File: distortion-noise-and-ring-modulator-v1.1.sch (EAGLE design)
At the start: 74 parts, among them IC1 TL074JT, IC4 LM13700SL, IC5 TL074JT, Q1 MMBT3906, T1 NOISE-2N3904, U1 MC1496DR2G, X1 MA07-1JN, X4 MA07-1JN

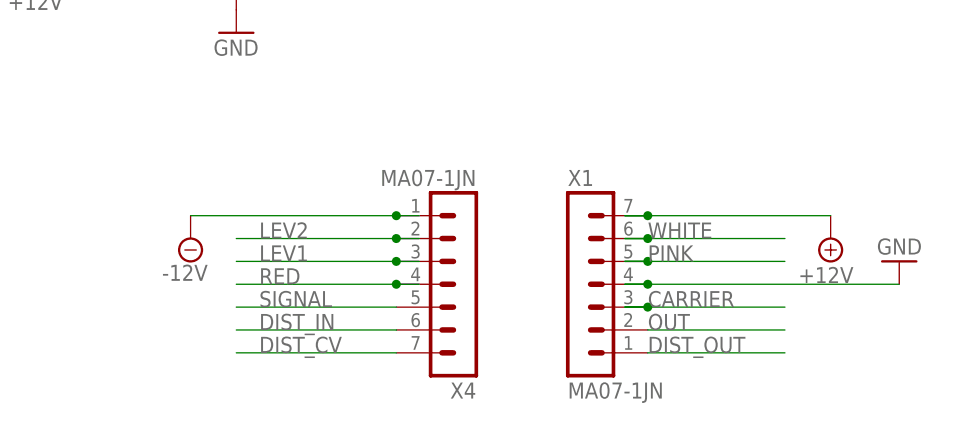
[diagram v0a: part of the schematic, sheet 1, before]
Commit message: Removed all external trimmers
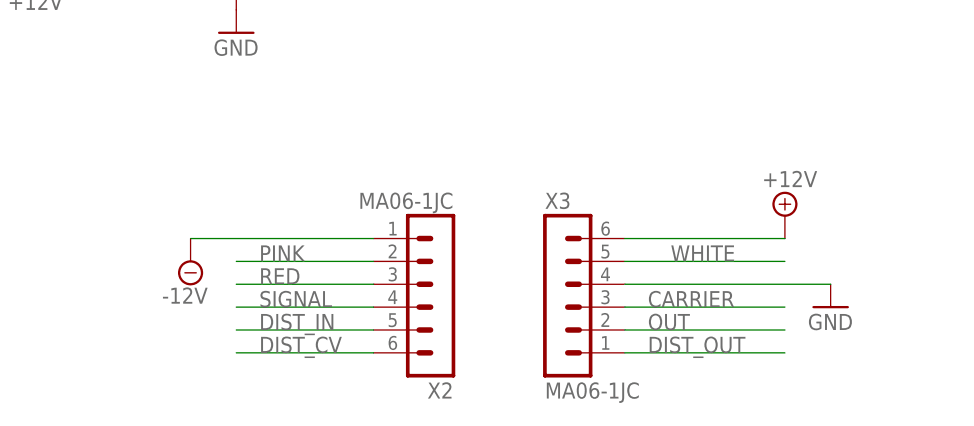
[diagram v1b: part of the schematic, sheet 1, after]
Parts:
- removed X1, X4: MA07-1JN, joakim:MA07-1JN
- added X2, X3: MA06-1JC, joakim:MA06-1JC
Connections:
- net +12V: now also X3.6; no longer X1.7
- net -12V: now also X2.1; no longer X4.1
- net CARRIER: now also X3.3; no longer X1.3
- net DIST_CV: now also X2.6; no longer X4.7
- net DIST_IN: now also X2.5; no longer X4.6
- net DIST_OUT: now also X3.1; no longer X1.1
- net GND: now also X3.4; no longer X1.4
- net LEV1: no longer X4.3
- net LEV2: no longer X4.2
- net OUT: now also X3.2; no longer X1.2
- net PINK: now also X2.2; no longer X1.5
- net RED: now also X2.3; no longer X4.4
- net SIGNAL: now also X2.4; no longer X4.5
- net WHITE: now also X3.5; no longer X1.6
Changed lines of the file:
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@@
 <part name="SUPPLY15" library="supply2" library_urn="urn:adsk.eagle:library:372" deviceset="-12V" device=""/>
 <part name="SUPPLY16" library="supply2" library_urn="urn:adsk.eagle:library:372" deviceset="+12V" device=""/>
-<part name="X1" library="joakim" deviceset="MA07-1J" device="N"/>
-<part name="X4" library="joakim" deviceset="MA07-1J" device="N"/>
+<part name="X2" library="joakim" deviceset="MA06-1J" device="C"/>
+<part name="X3" library="joakim" deviceset="MA06-1J" device="C"/>
 </parts>
 <sheets>
@@
 <attribute name="VALUE" x="-47.244" y="40.259" size="1.778" layer="96" rot="R180"/>
 </instance>
-<instance part="GND8" gate="1" x="180.34" y="27.94" smashed="yes" rot="R180">
-<attribute name="VALUE" x="182.88" y="30.48" size="1.778" layer="96" rot="R180"/>
+<instance part="GND8" gate="1" x="172.72" y="22.86" smashed="yes">
+<attribute name="VALUE" x="170.18" y="20.32" size="1.778" layer="96"/>
 </instance>
 <instance part="SUPPLY1" gate="+12V" x="-30.48" y="48.26" smashed="yes">
@@
 <attribute name="VALUE" x="78.74" y="66.675" size="1.778" layer="96"/>
 </instance>
-<instance part="SUPPLY9" gate="G$1" x="101.6" y="30.48" smashed="yes">
-<attribute name="VALUE" x="98.425" y="25.781" size="1.778" layer="96"/>
+<instance part="SUPPLY9" gate="G$1" x="101.6" y="27.94" smashed="yes">
+<attribute name="VALUE" x="98.425" y="23.241" size="1.778" layer="96"/>
 </instance>
 <instance part="SUPPLY10" gate="G$1" x="38.1" y="27.94" smashed="yes">
 <attribute name="VALUE" x="34.925" y="23.241" size="1.778" layer="96"/>
 </instance>
-<instance part="SUPPLY11" gate="+12V" x="172.72" y="30.48" smashed="yes" rot="R180">
-<attribute name="VALUE" x="175.26" y="27.305" size="1.778" layer="96" rot="R180"/>
+<instance part="SUPPLY11" gate="+12V" x="167.64" y="33.02" smashed="yes">
+<attribute name="VALUE" x="165.1" y="36.195" size="1.778" layer="96"/>
 </instance>
 <instance part="IC5" gate="B" x="139.7" y="71.12" smashed="yes">
@@
 <attribute name="VALUE" x="10.16" y="122.555" size="1.778" layer="96"/>
 </instance>
-<instance part="X1" gate="G$1" x="144.78" y="25.4" smashed="yes">
-<attribute name="VALUE" x="143.51" y="12.7" size="1.778" layer="96"/>
-<attribute name="NAME" x="143.51" y="36.322" size="1.778" layer="95"/>
-</instance>
-<instance part="X4" gate="G$1" x="132.08" y="25.4" smashed="yes" rot="R180">
-<attribute name="VALUE" x="133.35" y="38.1" size="1.778" layer="96" rot="R180"/>
-<attribute name="NAME" x="133.35" y="14.478" size="1.778" layer="95" rot="R180"/>
+<instance part="X2" gate="G$1" x="127" y="25.4" smashed="yes" rot="R180">
+<attribute name="VALUE" x="130.81" y="35.56" size="1.778" layer="96" rot="R180"/>
+<attribute name="NAME" x="130.81" y="14.478" size="1.778" layer="95" rot="R180"/>
+</instance>
+<instance part="X3" gate="G$1" x="144.78" y="22.86" smashed="yes">
+<attribute name="VALUE" x="140.97" y="12.7" size="1.778" layer="96"/>
+<attribute name="NAME" x="140.97" y="33.782" size="1.778" layer="95"/>
 </instance>
 </instances>
@@
 <segment>
 <pinref part="GND8" gate="1" pin="GND"/>
-<wire x1="180.34" y1="25.4" x2="152.4" y2="25.4" width="0.1524" layer="91"/>
-<wire x1="152.4" y1="25.4" x2="149.86" y2="25.4" width="0.1524" layer="91"/>
-<wire x1="149.86" y1="25.4" x2="152.4" y2="25.4" width="0.1524" layer="91"/>
-<pinref part="X1" gate="G$1" pin="4"/>
-<junction x="152.4" y="25.4"/>
+<wire x1="172.72" y1="25.4" x2="149.86" y2="25.4" width="0.1524" layer="91"/>
+<pinref part="X3" gate="G$1" pin="4"/>
 </segment>
 </net>
@@
 </segment>
 <segment>
-<wire x1="127" y1="33.02" x2="124.46" y2="33.02" width="0.1524" layer="91"/>
 <pinref part="SUPPLY9" gate="G$1" pin="-12V"/>
-<pinref part="X4" gate="G$1" pin="1"/>
-<wire x1="124.46" y1="33.02" x2="101.6" y2="33.02" width="0.1524" layer="91"/>
-<junction x="124.46" y="33.02"/>
+<wire x1="121.92" y1="30.48" x2="101.6" y2="30.48" width="0.1524" layer="91"/>
+<pinref part="X2" gate="G$1" pin="1"/>
 </segment>
 <segment>
@@
 </segment>
 <segment>
-<wire x1="152.4" y1="20.32" x2="167.64" y2="20.32" width="0.1524" layer="91"/>
 <label x="152.4" y="20.32" size="1.778" layer="95"/>
-<pinref part="X1" gate="G$1" pin="2"/>
+<pinref part="X3" gate="G$1" pin="2"/>
+<wire x1="149.86" y1="20.32" x2="167.64" y2="20.32" width="0.1524" layer="91"/>
 </segment>
 </net>
@@
 <segment>
 <label x="152.4" y="22.86" size="1.778" layer="95"/>
-<wire x1="167.64" y1="22.86" x2="152.4" y2="22.86" width="0.1524" layer="91"/>
-<wire x1="152.4" y1="22.86" x2="149.86" y2="22.86" width="0.1524" layer="91"/>
-<wire x1="149.86" y1="22.86" x2="152.4" y2="22.86" width="0.1524" layer="91"/>
-<pinref part="X1" gate="G$1" pin="3"/>
-<junction x="152.4" y="22.86"/>
+<wire x1="167.64" y1="22.86" x2="149.86" y2="22.86" width="0.1524" layer="91"/>
+<pinref part="X3" gate="G$1" pin="3"/>
 </segment>
 </net>
@@
 </segment>
 <segment>
-<wire x1="106.68" y1="22.86" x2="124.46" y2="22.86" width="0.1524" layer="91"/>
+<wire x1="106.68" y1="22.86" x2="121.92" y2="22.86" width="0.1524" layer="91"/>
 <label x="109.22" y="22.86" size="1.778" layer="95"/>
-<pinref part="X4" gate="G$1" pin="5"/>
+<pinref part="X2" gate="G$1" pin="4"/>
 </segment>
 </net>
@@
 </segment>
 <segment>
-<wire x1="172.72" y1="33.02" x2="152.4" y2="33.02" width="0.1524" layer="91"/>
+<wire x1="167.64" y1="30.48" x2="149.86" y2="30.48" width="0.1524" layer="91"/>
 <pinref part="SUPPLY11" gate="+12V" pin="+12V"/>
-<wire x1="152.4" y1="33.02" x2="149.86" y2="33.02" width="0.1524" layer="91"/>
-<wire x1="149.86" y1="33.02" x2="152.4" y2="33.02" width="0.1524" layer="91"/>
-<pinref part="X1" gate="G$1" pin="7"/>
-<junction x="152.4" y="33.02"/>
+<pinref part="X3" gate="G$1" pin="6"/>
 </segment>
 <segment>
@@
 </segment>
 </net>
-<net name="LEV2" class="0">
-<segment>
-<wire x1="127" y1="30.48" x2="124.46" y2="30.48" width="0.1524" layer="91"/>
-<label x="109.22" y="30.48" size="1.778" layer="95"/>
-<pinref part="X4" gate="G$1" pin="2"/>
-<wire x1="124.46" y1="30.48" x2="106.68" y2="30.48" width="0.1524" layer="91"/>
-<junction x="124.46" y="30.48"/>
-</segment>
-</net>
-<net name="LEV1" class="0">
-<segment>
-<wire x1="127" y1="27.94" x2="124.46" y2="27.94" width="0.1524" layer="91"/>
+<net name="RED" class="0">
+<segment>
+<label x="109.22" y="25.4" size="1.778" layer="95"/>
+<pinref part="X2" gate="G$1" pin="3"/>
+<wire x1="121.92" y1="25.4" x2="106.68" y2="25.4" width="0.1524" layer="91"/>
+</segment>
+</net>
+<net name="WHITE" class="0">
+<segment>
+<label x="154.94" y="27.94" size="1.778" layer="95"/>
+<wire x1="149.86" y1="27.94" x2="167.64" y2="27.94" width="0.1524" layer="91"/>
+<pinref part="X3" gate="G$1" pin="5"/>
+</segment>
+</net>
+<net name="DIST_IN" class="0">
+<segment>
+<label x="109.22" y="20.32" size="1.778" layer="95"/>
+<pinref part="X2" gate="G$1" pin="5"/>
+<wire x1="121.92" y1="20.32" x2="106.68" y2="20.32" width="0.1524" layer="91"/>
+</segment>
+</net>
+<net name="DIST_OUT" class="0">
+<segment>
+<label x="152.4" y="17.78" size="1.778" layer="95"/>
+<pinref part="X3" gate="G$1" pin="1"/>
+<wire x1="149.86" y1="17.78" x2="167.64" y2="17.78" width="0.1524" layer="91"/>
+</segment>
+</net>
+<net name="DIST_CV" class="0">
+<segment>
+<label x="109.22" y="17.78" size="1.778" layer="95"/>
+<pinref part="X2" gate="G$1" pin="6"/>
+<wire x1="121.92" y1="17.78" x2="106.68" y2="17.78" width="0.1524" layer="91"/>
+</segment>
+</net>
+<net name="PINK" class="0">
+<segment>
+<wire x1="106.68" y1="27.94" x2="121.92" y2="27.94" width="0.1524" layer="91"/>
 <label x="109.22" y="27.94" size="1.778" layer="95"/>
-<pinref part="X4" gate="G$1" pin="3"/>
-<wire x1="124.46" y1="27.94" x2="106.68" y2="27.94" width="0.1524" layer="91"/>
-<junction x="124.46" y="27.94"/>
-</segment>
-</net>
-<net name="RED" class="0">
-<segment>
-<wire x1="127" y1="25.4" x2="124.46" y2="25.4" width="0.1524" layer="91"/>
-<label x="109.22" y="25.4" size="1.778" layer="95"/>
-<pinref part="X4" gate="G$1" pin="4"/>
-<wire x1="124.46" y1="25.4" x2="106.68" y2="25.4" width="0.1524" layer="91"/>
-<junction x="124.46" y="25.4"/>
-</segment>
-</net>
-<net name="WHITE" class="0">
-<segment>
-<wire x1="149.86" y1="30.48" x2="152.4" y2="30.48" width="0.1524" layer="91"/>
-<label x="152.4" y="30.48" size="1.778" layer="95"/>
-<wire x1="152.4" y1="30.48" x2="167.64" y2="30.48" width="0.1524" layer="91"/>
-<wire x1="149.86" y1="30.48" x2="152.4" y2="30.48" width="0.1524" layer="91"/>
-<pinref part="X1" gate="G$1" pin="6"/>
-<junction x="152.4" y="30.48"/>
-</segment>
-</net>
-<net name="PINK" class="0">
-<segment>
-<wire x1="149.86" y1="27.94" x2="152.4" y2="27.94" width="0.1524" layer="91"/>
-<label x="152.4" y="27.94" size="1.778" layer="95"/>
-<wire x1="152.4" y1="27.94" x2="167.64" y2="27.94" width="0.1524" layer="91"/>
-<wire x1="149.86" y1="27.94" x2="152.4" y2="27.94" width="0.1524" layer="91"/>
-<pinref part="X1" gate="G$1" pin="5"/>
-<junction x="152.4" y="27.94"/>
-</segment>
-</net>
-<net name="DIST_IN" class="0">
-<segment>
-<wire x1="124.46" y1="20.32" x2="106.68" y2="20.32" width="0.1524" layer="91"/>
-<label x="109.22" y="20.32" size="1.778" layer="95"/>
-<pinref part="X4" gate="G$1" pin="6"/>
-</segment>
-</net>
-<net name="DIST_OUT" class="0">
-<segment>
-<wire x1="152.4" y1="17.78" x2="167.64" y2="17.78" width="0.1524" layer="91"/>
-<label x="152.4" y="17.78" size="1.778" layer="95"/>
-<pinref part="X1" gate="G$1" pin="1"/>
-</segment>
-</net>
-<net name="DIST_CV" class="0">
-<segment>
-<wire x1="124.46" y1="17.78" x2="106.68" y2="17.78" width="0.1524" layer="91"/>
-<label x="109.22" y="17.78" size="1.778" layer="95"/>
-<pinref part="X4" gate="G$1" pin="7"/>
-</segment>
-</net>
+<pinref part="X2" gate="G$1" pin="2"/>
+</segment>
+</net>

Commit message: Nude pin headers
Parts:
- X2, X3: value MA06-1JC -> MA06-1JN; device joakim:MA06-1JC -> joakim:MA06-1JN
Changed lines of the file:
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@@
 <part name="SUPPLY15" library="supply2" library_urn="urn:adsk.eagle:library:372" deviceset="-12V" device=""/>
 <part name="SUPPLY16" library="supply2" library_urn="urn:adsk.eagle:library:372" deviceset="+12V" device=""/>
-<part name="X2" library="joakim" deviceset="MA06-1J" device="C"/>
-<part name="X3" library="joakim" deviceset="MA06-1J" device="C"/>
+<part name="X2" library="joakim" deviceset="MA06-1J" device="N" value="MA06-1JN"/>
+<part name="X3" library="joakim" deviceset="MA06-1J" device="N" value="MA06-1JN"/>
 </parts>
 <sheets>
